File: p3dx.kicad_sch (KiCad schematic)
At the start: 0 parts

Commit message: Simplified sheet tree; fixed all labels
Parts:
- added C18: ~, symbol Device:C
- added D3: T4, symbol Device:D
- added J12: IR2, symbol Connector_Generic:Conn_01x03
- added J18: IR3, symbol Connector_Generic:Conn_01x03
- added J19: Unlabeled, symbol Connector_Generic:Conn_01x08
- added J28: H8 MICRO-CONTROLLER, symbol Connector_Generic:Conn_02x13_Odd_Even
- added J30: Charger, symbol Connector_Generic:Conn_01x02
- added J37: Cooling Fan, symbol Connector_Generic:Conn_01x02
- added J38: Unlabeled, symbol Connector_Generic:Conn_01x04
- added J8: IR0, symbol Connector_Generic:Conn_01x03
- added J9: IR1, symbol Connector_Generic:Conn_01x03
- added JP3: LEFT ENCODER, symbol Connector_Generic:Conn_02x05_Odd_Even
- added JP4: RIGHT ENCODER, symbol Connector_Generic:Conn_02x05_Odd_Even
- added Q10, Q9: NPN, symbol Simulation_SPICE:NPN
- added R46, R68: 20k, symbol Device:R
- added R47, R58, R67: 10k, symbol Device:R
- added R52: 10.3k, symbol Device:R
- added R57, R70: 4.7k, symbol Device:R
- added R61: 0, symbol Device:R
- added R64, R73, R75: 3k, symbol Device:R
- added R65, R72, R74: 12k, symbol Device:R
- added R66: 510, symbol Device:R
- added R69: 15k, symbol Device:R
- added R71: 2.2k, symbol Device:R
- added R77, R78: ~, symbol Device:R
- added U10, U9: TS922I, symbol Device:Opamp_Dual
- added U11: LM35DT, Package_TO_SOT_THT:TO-220-3_Vertical, symbol Sensor_Temperature:LM35-NEB
- added U3: 74HC14, Package_DIP:DIP-14_W7.62mm_SMDSocket_SmallPads, symbol 74xx:74HC14
- added U7: PT78ST105V, symbol Pioneer:PT78ST105V
- added U8: 74HC14, symbol 74xx:74HC14
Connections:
- new net: J28.22 (Pin_22), R46.1, R47.2
- new net: U3.10, U8.13
- new net: D3.2 (A), R57.1
- new net: R72.1, R77.1, U10.1
- new net: R67.1, R70.1, U9.1
- new net: R66.1, R67.2, U9.3 (+)
- new net: Q10.2 (B), R70.2, R71.1
- new net: J30.1 (Pin_1), R58.2
- new net: JP4.1 (Pin_1), U3.5
- new net: Q9.1 (C), R58.1
- new net: R65.1, R66.2, U9.7
- new net: R64.1, R65.2, U9.6 (-)
- new net: R68.2, R69.1, U9.2 (-)
- new net: U11.3 (V_{OUT}), U9.5 (+)
- new net: JP4.8 (Pin_8), U3.9
- new net: R74.2, R75.1, U10.6 (-)
- new net: R74.1, R78.1, U10.7
- new net: U3.12, U8.5
- new net: JP3.1 (Pin_1), U3.1
- new net: JP3.8 (Pin_8), U3.3
- new net: R72.2, R73.1, U10.2 (-)
- new net: J37.2 (Pin_2), Q10.1 (C)
- new net: R52.1, U8.2, U8.4
- new net +12V: J37.1 (Pin_1), R46.2
- new net +5V: C18.2, J38.1 (Pin_1), JP3.2 (Pin_2), JP4.2 (Pin_2), R57.2, R68.1, U10.8 (V+), U11.1 (+V_{S}), U3.14 (VCC), U7.1 (IN), U8.14 (VCC), U9.8 (V+)
- new net 5V_REG: J12.1 (Pin_1), J18.1 (Pin_1), J8.1 (Pin_1), J9.1 (Pin_1), U7.3 (OUT)
- new net AN1: J28.24 (Pin_24), R77.2
- new net AN2: J28.26 (Pin_26), R78.2
- new net C9_(Left_Drv): R61.1
- new net CC: D3.1 (K), J28.13 (Pin_13), Q9.2 (B)
- new net EL1: U3.2
- new net EL2: U3.4
- new net ER1: U3.8
- new net ER2: U3.6
- new net GND: C18.1, J12.3 (Pin_3), J18.3 (Pin_3), J19.5 (Pin_5), J19.6 (Pin_6), J19.7 (Pin_7), J19.8 (Pin_8), J28.23 (Pin_23), J28.25 (Pin_25), J28.7 (Pin_7), J30.2 (Pin_2), J38.4 (Pin_4), J8.3 (Pin_3), J9.3 (Pin_3), JP3.6 (Pin_6), JP4.6 (Pin_6), Q10.3 (E), Q9.3 (E), R47.1, R52.2, R61.2, R64.2, R69.2, R71.2, R73.2, R75.2, U10.4 (V-), U11.2 (GND), U3.7 (GND), U7.2 (GND), U8.1, U8.11, U8.3, U8.7 (GND), U9.4 (V-)
- new net IR0: J28.20 (Pin_20), J8.2 (Pin_2)
- new net IR1: J28.21 (Pin_21), J9.2 (Pin_2)
- new net IR2: J12.2 (Pin_2), J28.18 (Pin_18)
- new net IR3: J18.2 (Pin_2), J28.19 (Pin_19)
- new net IR4: J19.1 (Pin_1), J28.16 (Pin_16)
- new net IR5: J19.2 (Pin_2), J28.17 (Pin_17)
- new net IR6: J19.3 (Pin_3), J28.14 (Pin_14)
- new net IR7: J19.4 (Pin_4), J28.15 (Pin_15)
- new net LE1: J28.6 (Pin_6)
- new net LE2: J28.12 (Pin_12)
- new net LMC1: J28.1 (Pin_1), U3.11
- new net LMT: J38.2 (Pin_2), U10.3 (+)
- new net Left_C1: U8.12
- new net Q12,R50_Switched_Radio: J28.9 (Pin_9)
- new net Q13,_R54: J28.11 (Pin_11)
- new net R13: J28.2 (Pin_2)
- new net RE1: J28.8 (Pin_8)
- new net RE2: J28.10 (Pin_10)
- new net RMC1: J28.3 (Pin_3), U3.13
- new net RMT: J38.3 (Pin_3), U10.5 (+)
- new net Right_C1: U8.6
- new net Right_C2: J28.4 (Pin_4)
- new net U1_LEFT_DRIVER: U8.9
- new net U8A_2,U8B_4: J28.5 (Pin_5)
- no-connect marks 0 -> 16
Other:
- removed sheet Buffers and Connectors
- removed sheet Miscellanea
- added sheet Left Driver (driver_l.kicad_sch)
- note added: "R77 = LMOT TEMP"
- note added: "R78 = RMOT TEMP"
- company: (none) -> CC0-1.0 License
- title: (none) -> Pioneer 3-DX Motor Control Board

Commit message: Add IRF5303 symbol and datasheet Add power distribution and generation Fix several issues related to power distribution Rework unused buffers Fix grounding and pull-downs
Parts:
- removed U8: 74HC14, Package_DIP:DIP-14_W7.62mm_SMDSocket_SmallPads, symbol 74xx:74HC14
- added C19: ~, symbol Device:C
- added J10: Switched Radio, symbol Connector_Generic:Conn_01x03
- added Q12, Q13: NPN, symbol Simulation_SPICE:NPN
- added Q17, Q18, Q19, Q20: IRF5305, symbol Pioneer:IRF5305
- added R48, R50, R51, R54: 4.7k, symbol Device:R
- added R49, R53: 10k, symbol Device:R
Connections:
- net C9_(Left_Drv) is gone; now on net GND: R61.1
- net U8A_2,U8B_4 is gone; now on net PD1: J28.5 (Pin_5)
- net +5V: now also U7.3 (OUT), C19.2, Q17.3 (S), Q19.3 (S), R48.1, R50.2, R51.1, R54.2; no longer U7.1 (IN)
- net GND: now also U8.10, U8.8, C19.1, J10.2 (Pin_2); no longer R61.2
- net PD1: now reaches R52.1, U8.2, U8.4
- net 5V_REG renamed +24V
- net +24V: now also U7.1 (IN), Q18.3 (S), Q20.3 (S), R49.2, R53.2; no longer U7.3 (OUT)
- net Q12,R50_Switched_Radio renamed RSW
- net RSW: now also Q12.3 (E), Q17.1 (G), R50.1
- net Q13,_R54 renamed PSW
- net PSW: now also Q13.3 (E), Q19.1 (G), R54.1
- net R13 renamed Left_C2
- net U1_LEFT_DRIVER renamed G1
- net G1: now also R61.2
- new net: Q13.1 (C), Q18.1 (G), R53.1
- new net: J10.1 (Pin_1), Q17.2 (D)
- new net: Q13.2 (B), R51.2
- new net: Q12.1 (C), Q20.1 (G), R49.1
- new net: Q12.2 (B), R48.2
- new net: J10.3 (Pin_3), Q20.2 (D)
- new net +12VS: Q18.2 (D)
- new net +5VS: Q19.2 (D)
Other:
- note added: "C9"
- moved on the sheet: C18, D3, J12, J18, J19, J28, J30, J37, J38, J8, J9, JP3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

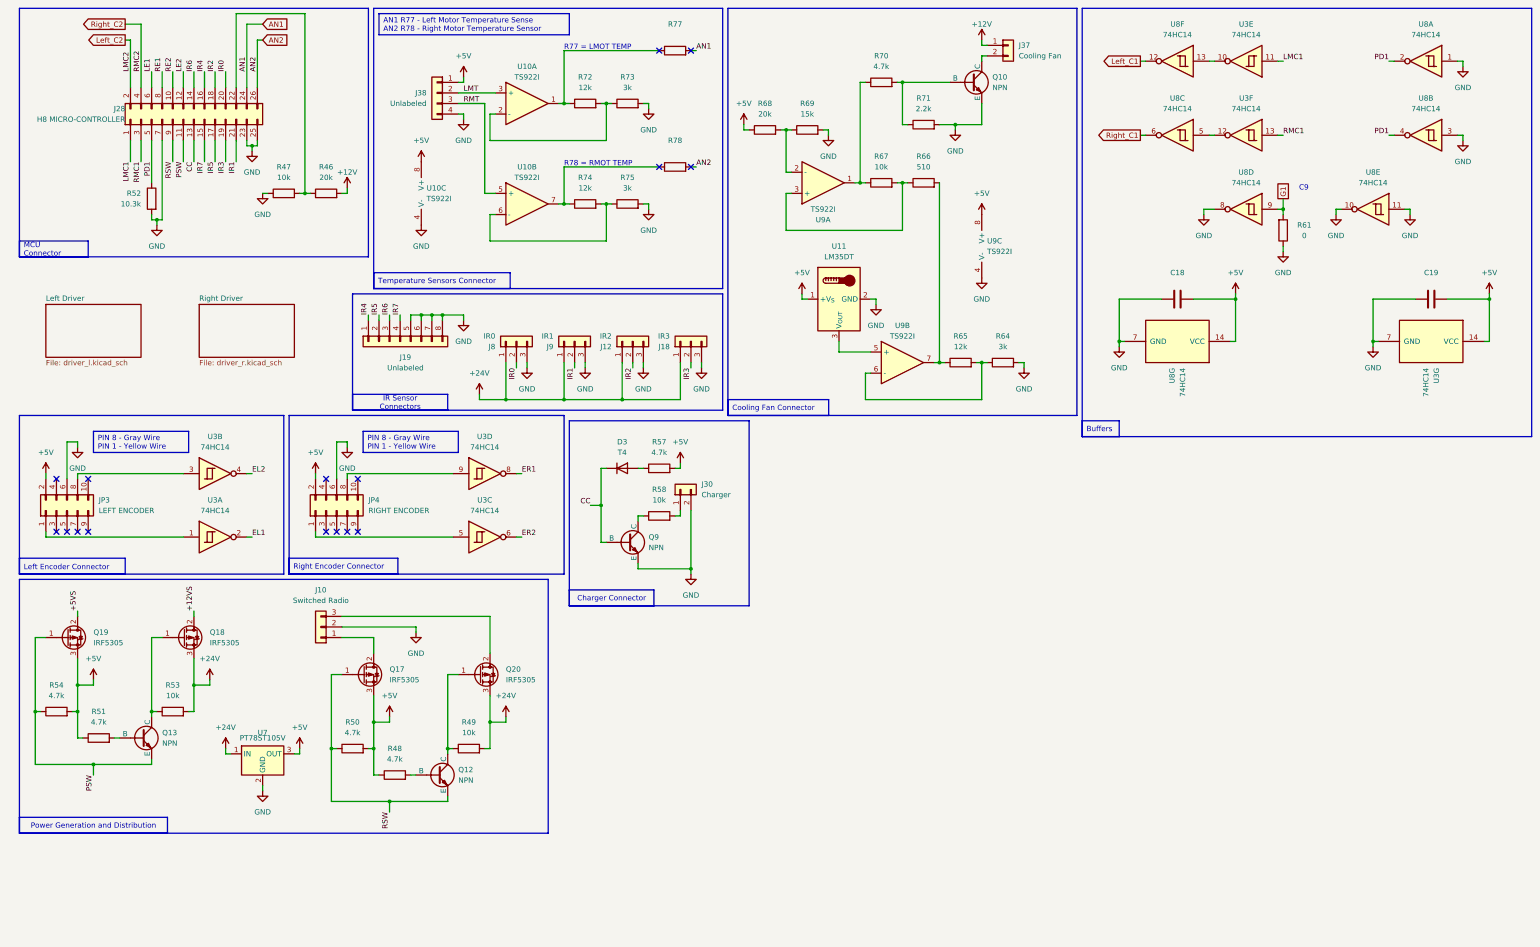
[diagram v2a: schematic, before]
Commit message: Fix main power distribution (+24V->+VBATT) and generation Use standard form for amplifiers Update date
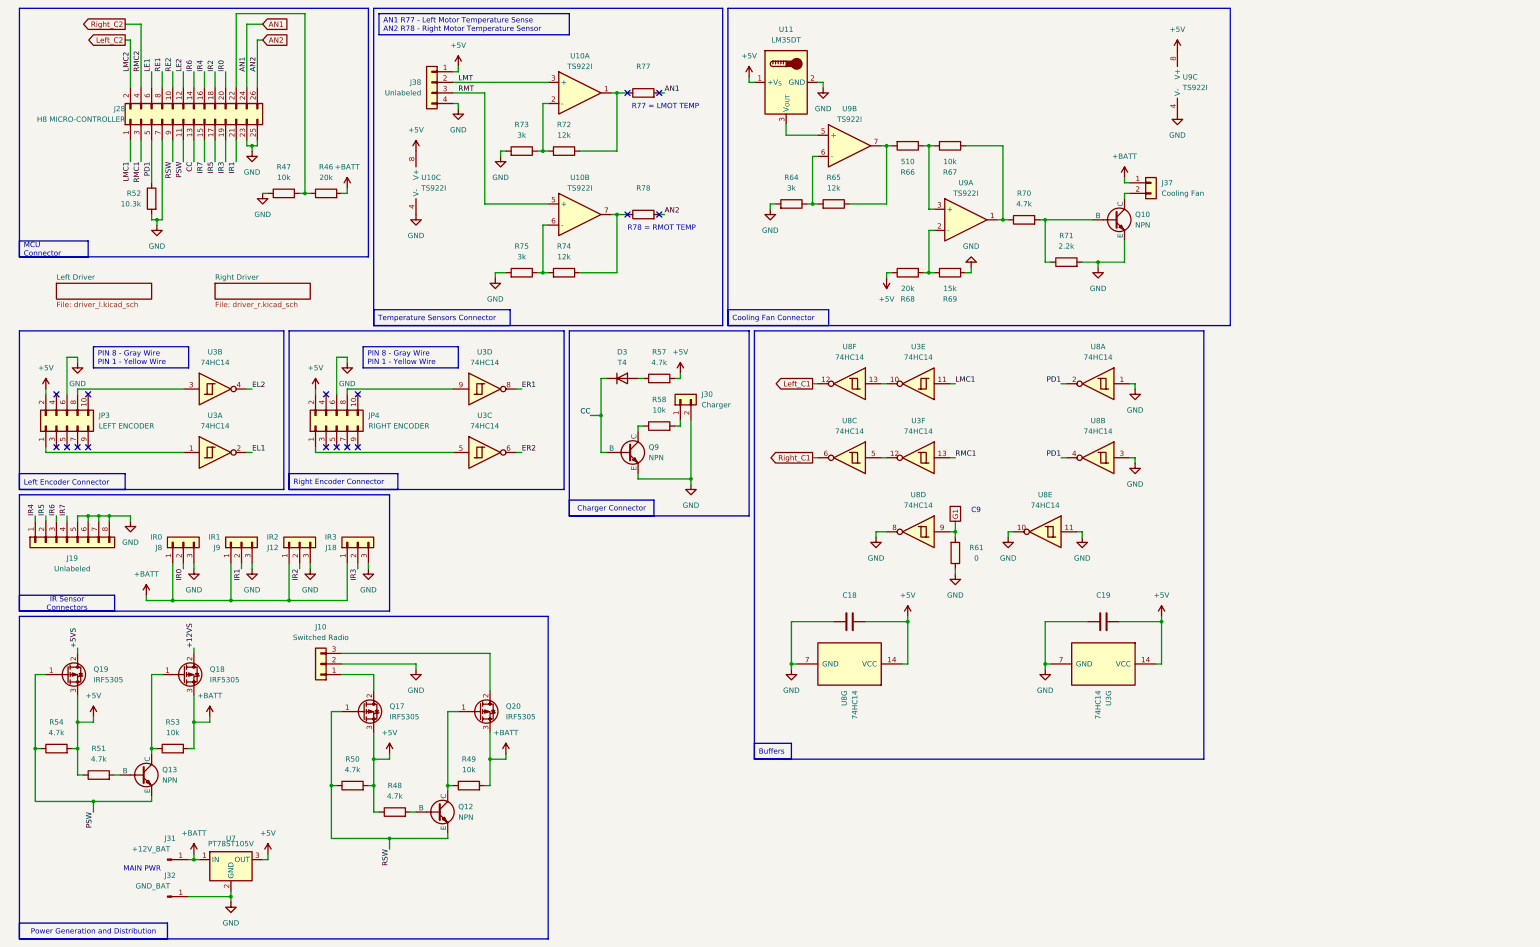
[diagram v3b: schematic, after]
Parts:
- added J31: +12V_BAT, symbol Connector:Conn_01x01_Pin
- added J32: GND_BAT, symbol Connector:Conn_01x01_Pin
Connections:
- net +24V is gone; now on net +BATT: J12.1 (Pin_1), J18.1 (Pin_1), J8.1 (Pin_1), J9.1 (Pin_1), Q18.3 (S), Q20.3 (S), R49.2, R53.2, U7.1 (IN)
- net GND: now also J32.1 (Pin_1)
- net +12V renamed +BATT
- net +BATT: now also J31.1 (Pin_1)
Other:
- note added: "MAIN PWR"
- moved on the sheet: C18, C19, D3, J10, J12, J18, J19, J30, J37, J38, J8, J9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

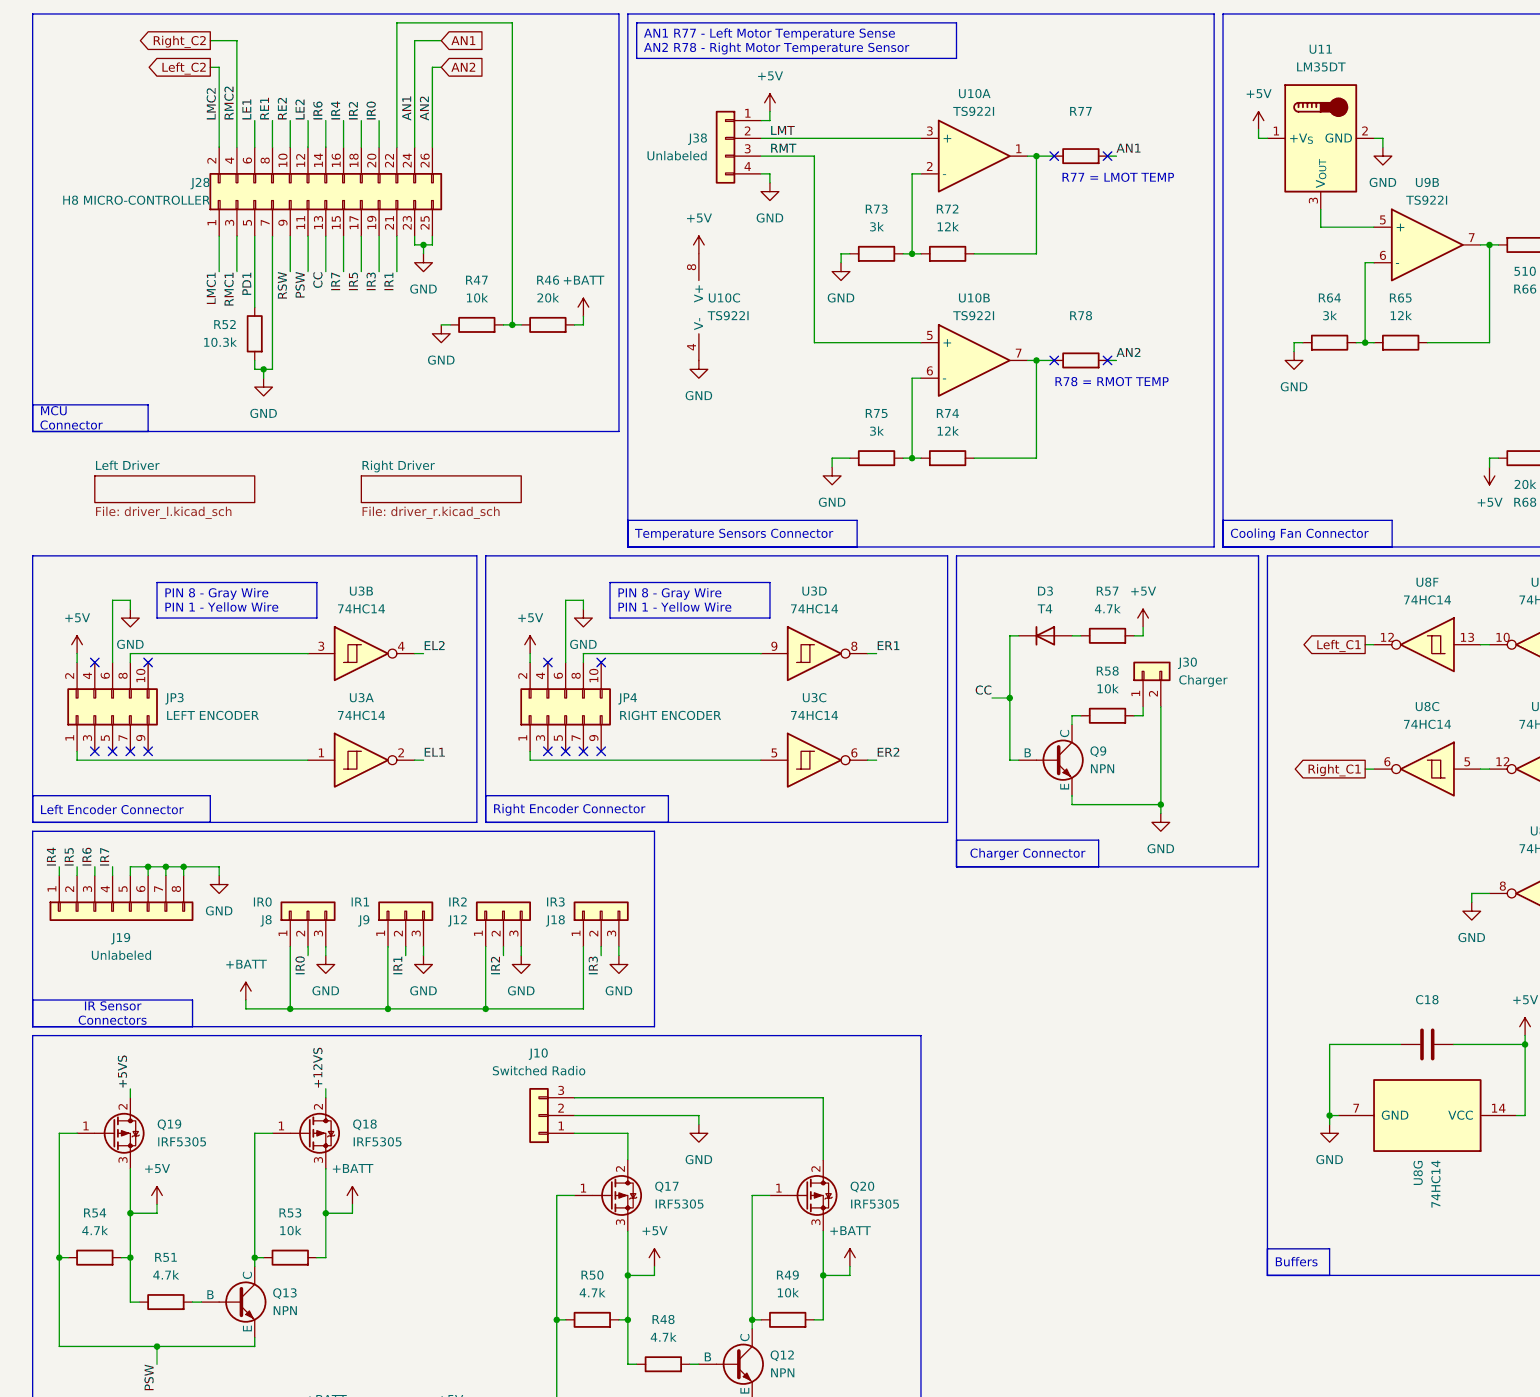
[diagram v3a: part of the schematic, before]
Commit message: Update driver motor scheme
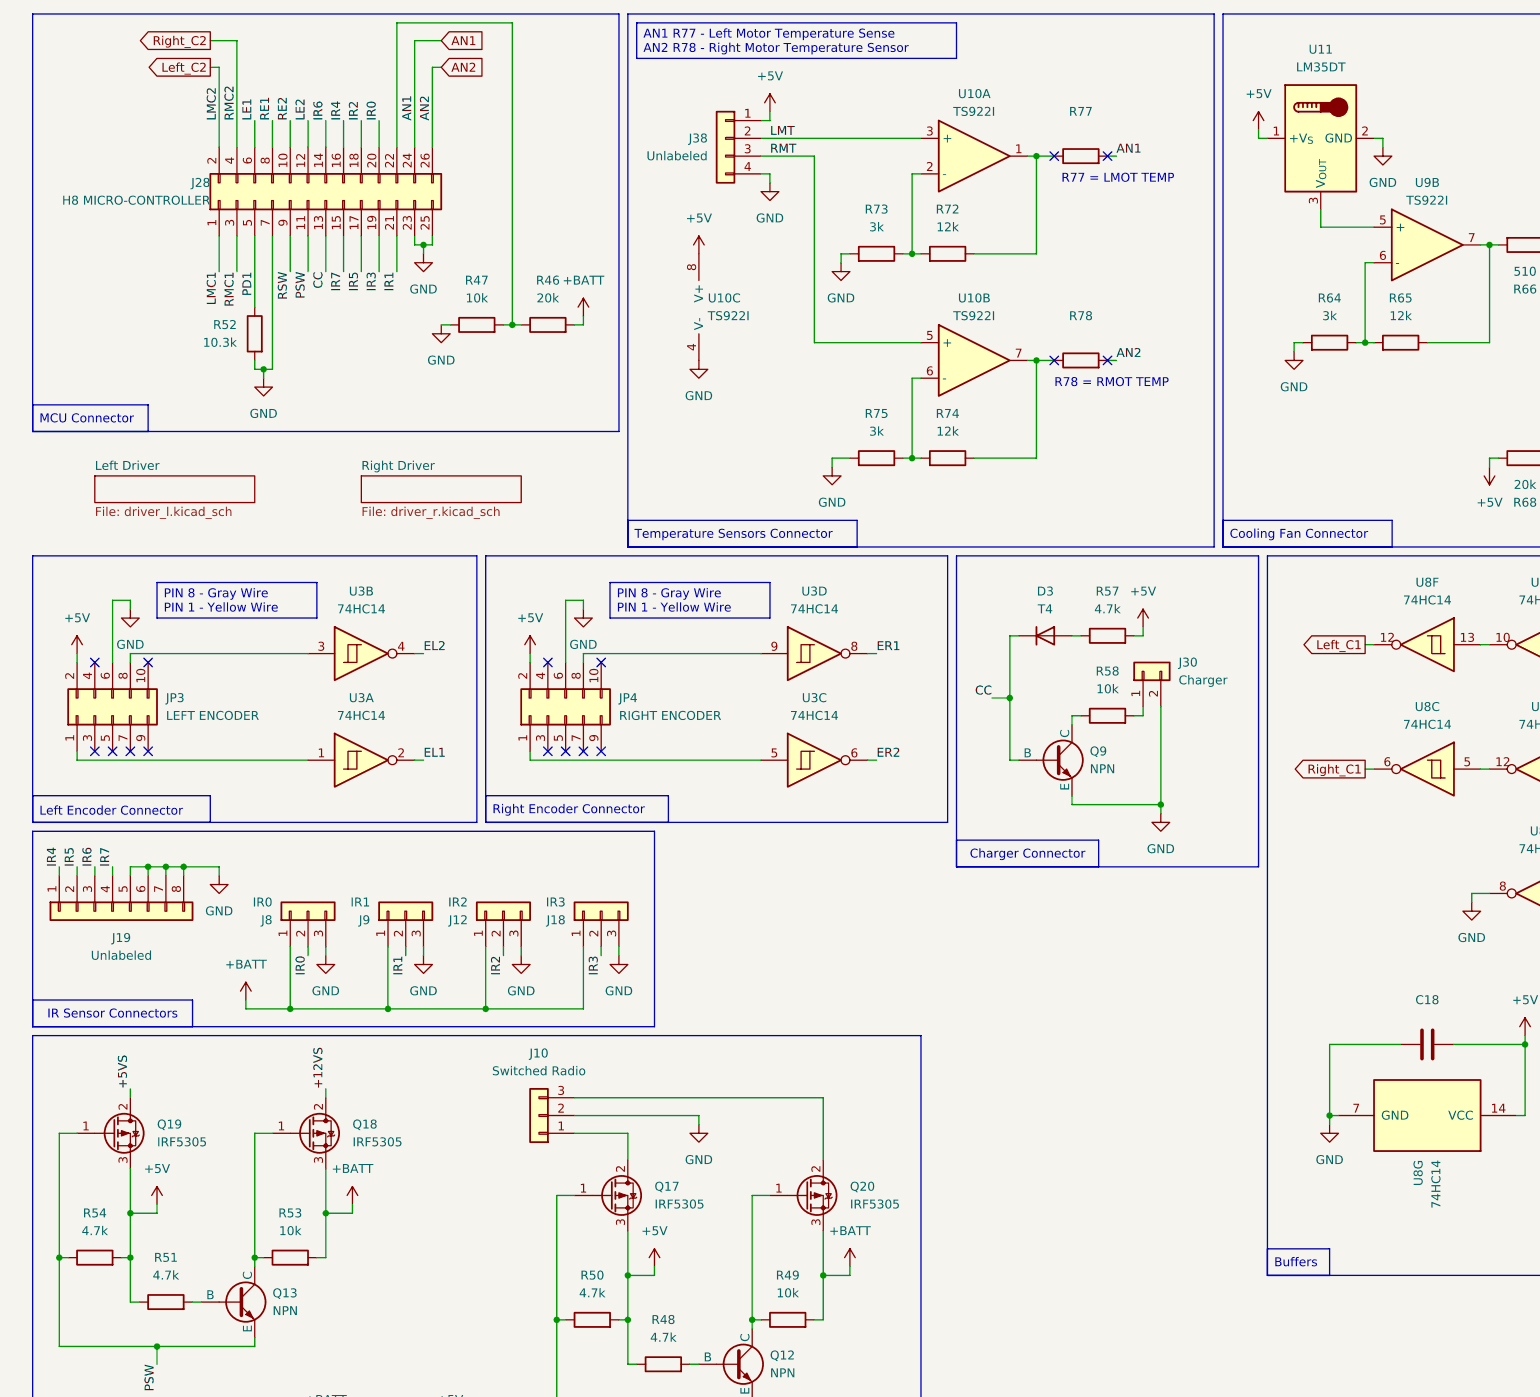
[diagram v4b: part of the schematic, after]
